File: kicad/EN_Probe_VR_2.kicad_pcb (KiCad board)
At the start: 2 copper layers, 34.9 x 22.9 mm, 25 parts, among them J2 Comment, J3 Comment, J4 Comment, J5 Comment, U1 3.3V REG, U2 2.8V REG, x5 MEMS

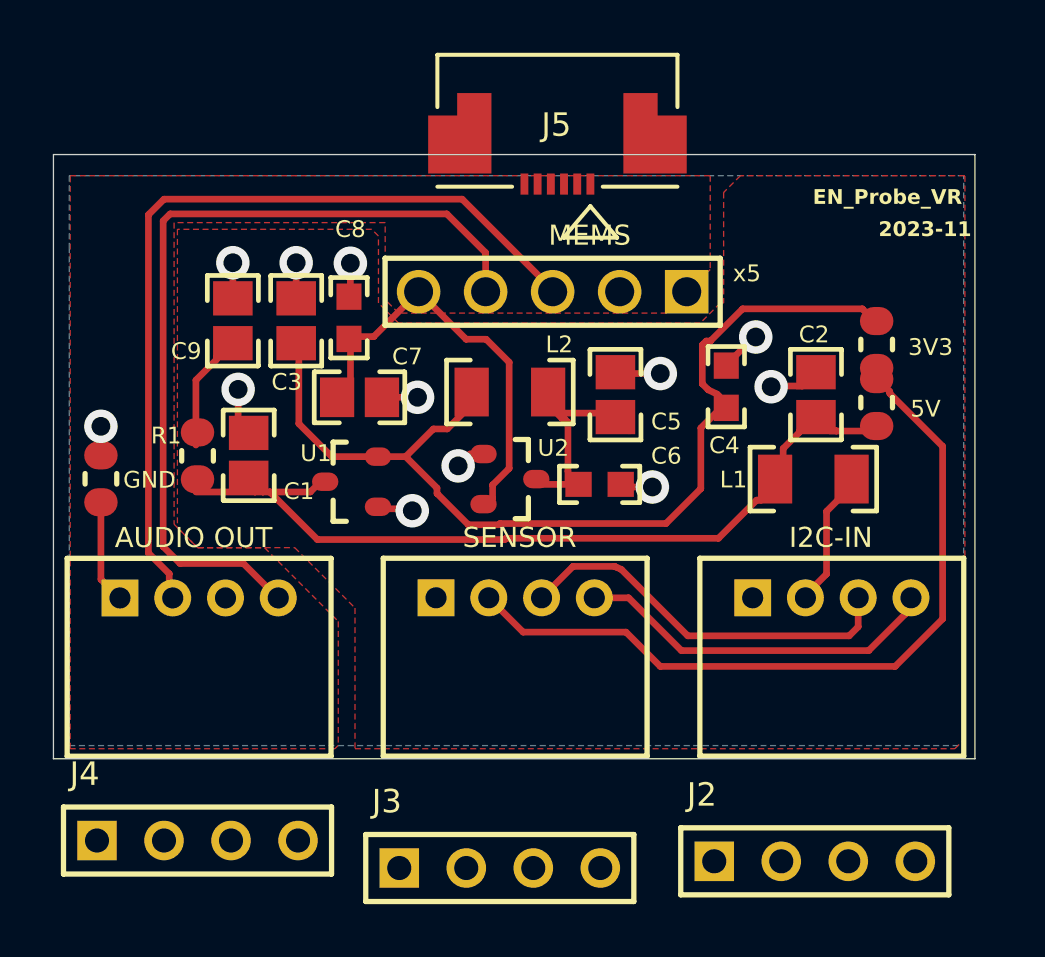
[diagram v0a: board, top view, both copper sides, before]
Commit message: EN_Probe_VR rev 2.00: verified KiCad conversion + ver 2.00 implementation
Goal 1 - conversion audit: verified the Altium->KiCad 10 conversion against the
Altium originals and repaired it: rebuilt footprint<->symbol links, created project
symbol/footprint libraries, converted ports to global labels, added power flags,
and resolved the value/MPN conflicts the Altium project carried internally
(C9 0.33uF, ferrite beads relabelled, U1 MPN, 0R jumpers). Closed with a
zero-mismatch schematic<->PCB cross-check.

Goal 2 - rev 2.00 implementation: new 34.925 x 25.4 mm outline, M2 mounting
holes, 2.54 mm headers with J3 reordered (SDA/SCL/GND/VCC), audio output RC
coupling (220R + 0.33uF + 39k per leg, fc ~12 Hz), 10k I2C pull-ups, 100 nF mic
bypass at the ZIF, solid two-layer ground, fully re-routed. Mic connector
corrected to the 8-circuit Molex 52745-0897 (the Infineon flex tail is 8 fingers
/ 4.5 mm and cannot enter the 6-circuit part; pinout: 2/7 GND, 4 OUT-, 5 OUT+,
6 VDD). Sensor VCC defaults to 3.3 V (R2 DNP, fit exactly one of R2/R3V3).

ERC 0/0, DRC 0, schematic parity 0, unconnected 0. Do not fabricate until the
flex continuity check confirms the connector pin mapping (V<->6, P<->5, N<->4,
G<->2 and 7 on a physical flex).
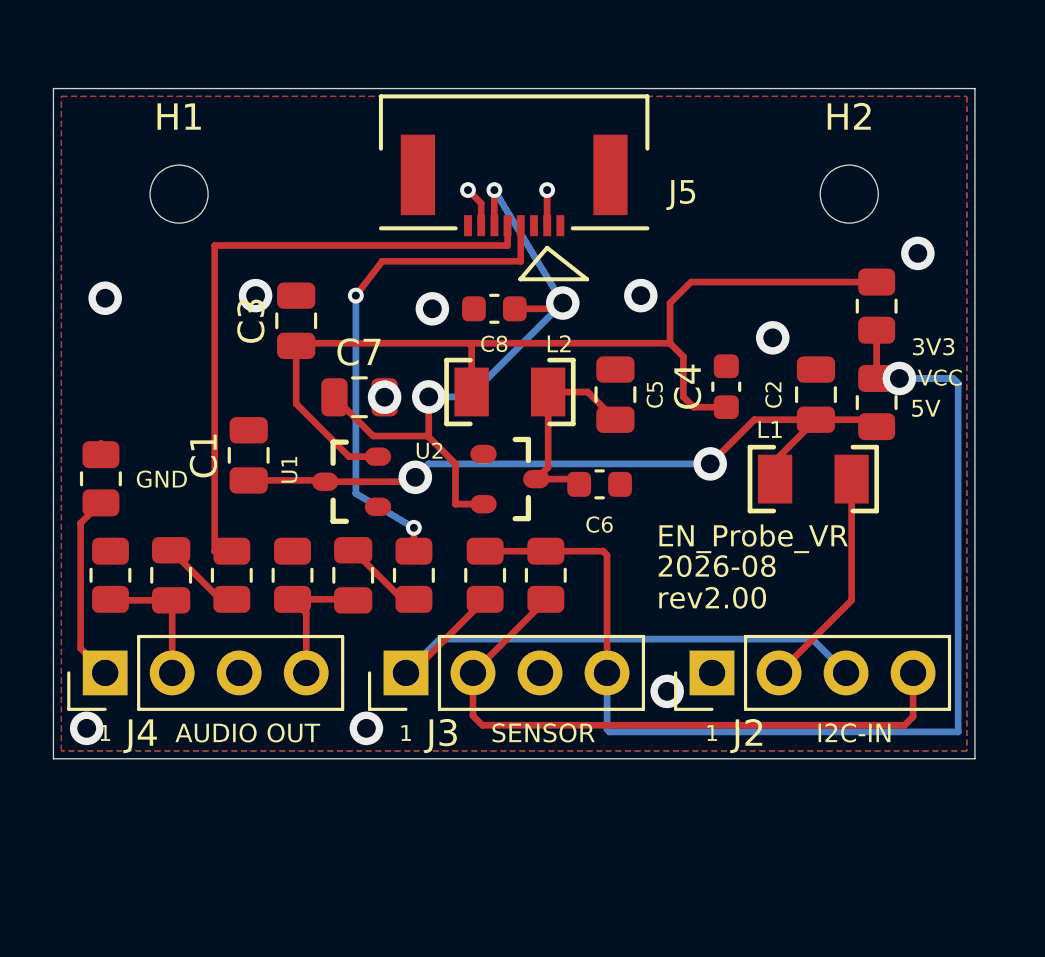
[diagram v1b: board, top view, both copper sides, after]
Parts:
- removed the J2 at (156.1, 120.3)
- removed the J3 at (144.1, 120.6)
- removed the J4 at (132.7, 119.6)
- removed x5: MEMS, Display adapter 20 to 20p4.5.2:HDR1X5
- added C10: 0.33uF, EN_Probe_VR_2:C_0805_2012Metric, F.Cu at (142.4, 109.5)
- added H1: M2, EN_Probe_VR_2:MountingHole_2.2mm_M2, F.Cu at (135.8, 95.1)
- added H2: M2, EN_Probe_VR_2:MountingHole_2.2mm_M2, F.Cu at (161.2, 95.1)
- added R4: 10k, EN_Probe_VR_2:R_0805_2012Metric, F.Cu at (147.4, 109.5)
- added R5: 10k, EN_Probe_VR_2:R_0805_2012Metric, F.Cu at (149.7, 109.5)
- added R6: 39k, EN_Probe_VR_2:R_0805_2012Metric, F.Cu at (133.2, 109.5)
- added R7: 220R, EN_Probe_VR_2:R_0805_2012Metric, F.Cu at (144.7, 109.5)
- added R8: 39k, EN_Probe_VR_2:R_0805_2012Metric, F.Cu at (140.1, 109.5)
- C1, C2, C3, C5, C7: footprint FerriteBead:0805 -> EN_Probe_VR_2:C_0805_2012Metric
- C4, C6, C8: footprint FerriteBead:0603 -> EN_Probe_VR_2:C_0603_1608Metric
- C9: value 680nF -> 0.33uF; footprint FerriteBead:0805 -> EN_Probe_VR_2:C_0805_2012Metric
- J2, J3, J4: renamed from ?; footprint EN_Probe_VR:HDRA1X4 2MM -> EN_Probe_VR_2:PinHeader_1x04_P2.54mm_Vertical
- J5: value Comment -> MEMS MIC; footprint 527450697:CON_527450697_ -> EN_Probe_VR_2:CON_527450897
- L1: value 2.2uH -> FB 160R; footprint FerriteBead:1206 -> EN_Probe_VR_2:1206
- L2: value 1.0uH -> FB 160R; footprint FerriteBead:1206 -> EN_Probe_VR_2:1206
- R1: value CRCW080522R0JNEA -> 220R; footprint SugarCube SCADng_R2.6 02:0805 -> EN_Probe_VR_2:R_0805_2012Metric
- R2: renamed from 5V; value CRCW080522R0JNEA -> 0R; footprint EN_Probe_VR:0805 -> EN_Probe_VR_2:R_0805_2012Metric
- R3: renamed from GND; value CRCW080522R0JNEA -> 0R; footprint EN_Probe_VR:0805 -> EN_Probe_VR_2:R_0805_2012Metric
- R3V3: renamed from 3V3; value CRCW080522R0JNEA -> 0R; footprint EN_Probe_VR:0805 -> EN_Probe_VR_2:R_0805_2012Metric
- U1, U2: footprint Display adapter 20 to 20p4.5.2:SOT23-3 -> EN_Probe_VR_2:SOT23-3
- moved C9 9.93 mm to (135.5, 109.5), turned to 90 degrees
- moved C8 5.52 mm to (147.8, 99.4), turned to 0 degrees
- moved R1 4.71 mm to (137.8, 109.5)
- moved J2 3.24 mm to (156.0, 113.2), turned to 90 degrees
- moved J3 3.07 mm to (144.4, 113.2), turned to 90 degrees
- moved J4 2.90 mm to (133.0, 113.2), turned to 90 degrees
- moved J5 2.27 mm to (148.5, 93.8)
- moved R3V3 1.45 mm to (162.2, 99.3)
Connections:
- net +3.3V renamed /+3.3V_FILT
- net NetC3_1 renamed +3.3VDC
- net NetJ2_2 renamed +5V in
- net NetJ4_1 renamed Net-(J4-Pad1)
- C1 pad 1: NetC1_1 -> +5V
- C2 pad 2: NetC1_1 -> +5V
- C7 pad 1: NetC7_1 -> +2.8VDC
- C8 pad 2: NetC7_1 -> +2.8VDC
- C9 pad 1: AGND -> Net-(C9-Pad1)
- C9 pad 2: NetC9_2 -> Net-(C9-Pad2)
- J2 pad 3: NetJ2_3 -> Net-(J2-Pad3)
- J2 pad 4: NetJ2_4 -> Net-(J2-Pad4)
- J3 pad 1: AGND -> Net-(J2-Pad3)
- J3 pad 2: NetJ3_2 -> Net-(J2-Pad4)
- J3 pad 3: NetJ2_3 -> AGND
- J3 pad 4: NetJ2_4 -> I2C VCC
- J4 pad 2: NetJ4_2 -> Net-(C9-Pad1)
- J4 pad 4: NetJ4_4 -> Net-(C10-Pad2)
- J5 pad 1: (no net) -> unconnected-(J5-Pad1)
- J5 pad 2: (no net) -> AGND
- J5 pad 3: (no net) -> unconnected-(J5-Pad3)
- J5 pad 4: (no net) -> Net-(J5-Pad4)
- J5 pad 5: (no net) -> Net-(J5-Pad5)
- J5 pad 6: (no net) -> +2.8VDC
- J5 pad P1: (no net) -> unconnected-(J5-PadP1)
- J5 pad P2: (no net) -> unconnected-(J5-PadP2)
- L1 pad 1: NetC1_1 -> +5V
- R1 pad 1: NetC9_2 -> Net-(J5-Pad5)
- R1 pad 2: NetC1_1 -> Net-(C9-Pad2)
- R2 pad 1: NetJ3_2 -> I2C VCC
- R2 pad 2: NetC1_1 -> +5V
- R3V3 pad 1: NetJ3_2 -> I2C VCC
- U1 pad 3: NetC1_1 -> +5V
- U2 pad 2: NetC7_1 -> +2.8VDC
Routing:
- net I2C VCC: track 0.00 -> 42.2 mm, vias 0 -> 1
- net NetC1_1: track 33.2 -> 0.00 mm
- net NetJ4_2: track 32.0 -> 0.00 mm
- net NetJ4_4: track 31.9 -> 0.00 mm
- net NetJ3_2: track 30.3 -> 0.00 mm
- net +5V: track 0.00 -> 27.8 mm, vias 0 -> 2
- net +2.8VDC: track 0.00 -> 24.5 mm, vias 0 -> 3
- net Net-(J2-Pad4): track 0.00 -> 24.2 mm
- net Net-(J5-Pad5): track 0.00 -> 23.9 mm
- net Net-(J2-Pad3): track 0.00 -> 21.9 mm
- net Net-(J5-Pad4): track 0.00 -> 19.2 mm, vias 0 -> 2
- net NetC7_1: track 16.5 -> 0.00 mm
- net NetJ2_3: track 14.9 -> 0.00 mm
- net NetJ2_4: track 14.0 -> 0.00 mm
- net AGND: track 16.9 -> 3.45 mm
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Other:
- board size 34.9 x 22.9 mm -> 34.9 x 25.4 mm
- rule solder_mask_min_width: 0.254 -> 0.1
- board text added: "1"
- board text added: "2026-08"
- board text added: "3V3"
- board text added: "5V"
- board text added: "AUDIO OUT"
- board text added: "GND"
- board text added: "I2C-IN"
- board text added: "SENSOR"
- board text added: "VCC"
- board text added: "rev2.00"
- board text removed: "2023-11"
